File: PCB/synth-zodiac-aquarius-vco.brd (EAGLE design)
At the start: 160 x 100 mm, 47 parts, among them J3 3P, Male, Breakaway, 2.54mm, Q1 PMP4201, SW1 SPDT, U3 LM393, U4 TL074A, U5 CD4066

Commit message: Snapshot of designs so far.
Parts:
- removed C12: 4700pF, rlc:0603-CAP
- removed C13: 3900pF, rlc:0603-CAP
- removed C14: 22uF, rlc:0603-CAP
- removed C15: 100pF, rlc:0603-CAP
- removed C16: 1.0uF, rlc:0603-CAP
- removed C17: 220pF, rlc:0603-CAP
- removed C18, C19, C20, C21: 0.1uF, rlc:0603-CAP
- removed D3, D4: 1N4148, diodes:SOD-123
- removed J3: 3P, Male, Breakaway, 2.54mm, con-headers:MA03X1-VT-THD
- removed JMP56, JMP59, JMP60, R27, R28: 0, rlc:0603-RES
- removed JMP61: NS, rlc:0603-RES
- removed R25: 4.99K, rlc:0603-RES
- removed SW1: SPDT, switch-thd:SS-12-F45
- removed VCO_CORE: TPTHD-038, con-testpoints:THD-038MIL-X1
- removed VR1: 10K, rlc:ALPS_RK09D113
- removed VR10, VR5: 100K, rlc:TRIM_BOURNS_TC33X
- added BIAS: NP, rlc:TRIM_BOURNS_TC33X
- added C1: 4700pF, rlc:0603-CAP
- added C10: 220pF, rlc:0603-CAP
- added C2: 22uF, rlc:0603-CAP
- added C3, C4, C6, C7: 0.1uF, rlc:0603-CAP
- added C5: 3900pF, rlc:0603-CAP
- added C8: 1.0uF, rlc:0603-CAP
- added C9: 100pF, rlc:0603-CAP
- added CONST1: Aquarius, circuit-monkey-zodiac:AQUARIUS-CONST
- added CP_EXP_VCO, CP_GND, CP_VCO_LIN_FM, CP_VCO_OUT: PADSMD-070X070, con-testpoints:SMD-070MIL
- added D1, D2: 1N4148, diodes:SOD-123
- added EXP_VCO_TRIM: 100K - NP, rlc:TRIM_BOURNS_TC33X
- added FREQ: 10K, rlc:POT-RV9110
- added GLYPH: Aquarius, circuit-monkey-zodiac:AQUARIUS-GLYPH
- added J1: (no value), con-jst:B4B-PH-SM4
- added KB_CV, PWM_CV, VCO_MOD_CV, VCO_OUT: 2-pin, VT, SMT, con-jst:B2B-PH-SM4
- added KB_TRIM: 100K, rlc:TRIM_BOURNS_TC33X
- added PCB: PCB FAB, circuit-monkey-zodiac:PENTAGON-40MM-RAD
- added R2, R3: 221K, rlc:0603-RES
- added R20, R21, R22: 4.99K, rlc:0603-RES
- added R5: 68.1K - NP, rlc:0603-RES
- added R8: 1.82M, rlc:0603-RES
- added SAW: TPSMD-040-RND, con-testpoints:SMD-040MIL-RND
- added TYPE: SPDT, switch-thd:SS-12-F45-PNL-SMT
- PULSE, TP4: value TPTHD-038 -> TPSMD-040-RND; device con-testpoints:THD-038MIL-X1 -> con-testpoints:SMD-040MIL-RND
- R10: value 2.2K -> 0
- R11: value 499K -> 0
- R12: value 1.82M -> NS
- R13: value 10K -> 0
- R14: value 4.75M -> 0
- R15: value 10.0K -> 100K
- R16: value 4.99K -> 100K
- R17: value 4.99K -> 10.0K
- R18: value 4.99K -> 4.75M
- R19: value 10K -> 4.99K
- R23: value 100K -> 10K
- R24: value 100K -> 0
- R4: value 221K -> 412K
- R6: value 412K -> 2.2K
- R7: value 221K -> 499K
- R9: value 68.1K -> 10K
- moved PULSE 92.5 mm to (47.8, 48.4), flipped to the bottom, turned to 180 degrees
- moved R4 92.4 mm to (30.0, 41.1), flipped to the bottom, turned to 180 degrees
- moved R24 88.4 mm to (45.7, 44.4), flipped to the bottom
- moved TP4 86.2 mm to (50.8, 22.3), flipped to the bottom, turned to 180 degrees
- moved R6 79.3 mm to (46.0, 23.1), flipped to the bottom, turned to 180 degrees
- moved R7 73.1 mm to (46.0, 18.6), flipped to the bottom
- moved R19 71.8 mm to (22.2, 29.9), flipped to the bottom, turned to 180 degrees
- moved R13 68.8 mm to (46.0, 15.2), flipped to the bottom, turned to 180 degrees
- moved R18 68.2 mm to (30.0, 21.8), flipped to the bottom
- moved R9 66.6 mm to (30.0, 17.8), flipped to the bottom
- moved R14 66.0 mm to (46.0, 16.5), flipped to the bottom, turned to 180 degrees
- moved R17 65.2 mm to (30.0, 27.1), flipped to the bottom
- moved R15 64.2 mm to (54.0, 13.1), flipped to the bottom
- moved R11 62.1 mm to (15.5, 26.1), flipped to the bottom, turned to 180 degrees
- moved R12 60.6 mm to (15.5, 23.5), flipped to the bottom
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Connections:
- removed net N$10: R4.1, VR1.2
- removed net N$11: C12.1, R10.1, R4.2, R6.2, R7.2, R9.2, U4.2
- removed net N$19: J3.2, R16.2, R17.1, R18.1
- new net BIAS: BIAS.C, R19.2, R20.1, R21.1
- new net FREQ: FREQ.C, R2.1
- new net FREQ_CV_MIX: C1.1, R2.2, R3.2, R4.2, R5.2, R6.1, U4.2
- net +5V: now also C2.2, C5.1, J1.3, R16.2, R22.1; no longer C13.1, C14.2, R24.2, R25.1
- net +9V: now also C10.2, C3.2, C6.2, C7.2, FREQ.T, J1.1; no longer C17.2, C18.2, C19.2, C21.2, VR1.3
- net -9V: now also C4.1, FREQ.B, J1.2, R8.1; no longer C20.1, R12.1, VR1.1
- net EXP_VCO_CV_IN: now also CP_EXP_VCO.1, EXP_VCO_TRIM.B; no longer VR5.B
- net EXP_VCO_LIN_FM: now also CP_VCO_LIN_FM.1, R7.1; no longer R11.1
- net GND: now also BIAS.B, C2.1, C3.1, C4.2, C6.1, C7.1, C8.1, CP_GND.1, D2.A, J1.4, KB_CV.2, PCB.MTG1, PCB.MTG2, PCB.MTG3, PCB.MTG4, PCB.MTG5, PWM_CV.2, R10.1, R11.1, R14.1, R20.2, R23.2, R9.1, TYPE.MTG1, TYPE.MTG2, VCO_MOD_CV.2, VCO_OUT.2; no longer C14.1, C16.1, C18.1, C19.1, C20.2, C21.1, D4.A, J3.1, JMP59.1, JMP60.1, R17.2, R19.2, R27.1, R28.1, SW1.MT1A, SW1.MT1B, SW1.MT1C, SW1.MT2A, SW1.MT2B, SW1.MT2C, VR1.MT1A, VR1.MT1B, VR1.MT1C, VR1.MT2A, VR1.MT2B, VR1.MT2C
- net KB_CV: now also KB_CV.1, KB_TRIM.B; no longer VR10.B
- net N$12: now also R7.2, R8.2; no longer R11.2, R12.2
- net N$14: now also C1.2, R6.2; no longer C12.2, R10.2
- net N$15: now also R12.2, R9.2; no longer JMP61.2, R13.2
- net N$16: now also C9.1, R17.1, R18.1; no longer C15.1, R14.1, R15.1
- net N$17: now also R14.2; no longer R27.2
- net N$18: now also C9.2, D1.A, R18.2; no longer C15.2, D3.A, R14.2
- net N$20: now also C5.2; no longer C13.2
- net N$21: now also BIAS.T, C8.2, R17.2, R19.1; no longer C16.2, J3.3, R15.2, R16.1
- net N$22: now also C10.1, R21.2; no longer C17.1, R18.2
- net N$23: now also R12.1; no longer JMP61.1
- net N$24: now also D1.K, D2.K, R23.1; no longer D3.K, D4.K, R19.1
- net N$25: now also R10.2; no longer JMP60.2
- net N$26: now also R11.2; no longer JMP59.2
- net N$27: now also R13.2; no longer R28.2
- net N$28: now also R15.2, R16.1; no longer R23.2, R24.1
- net N$29: now also TP4.TP; no longer TP4.1
- net N$8: now also KB_TRIM.C, KB_TRIM.T, R4.1; no longer R6.1, VR10.C, VR10.T
- net N$9: now also EXP_VCO_TRIM.C, EXP_VCO_TRIM.T, R5.1; no longer R9.1, VR5.C, VR5.T
- net PULSE: now also PULSE.TP, R22.2, TYPE.B; no longer PULSE.1, R25.2, SW1.B
- net PWM_CV: now also PWM_CV.1, R15.1; no longer R23.1
- net SAW: now also R24.2, TYPE.A; no longer JMP56.2, SW1.A
- net VCO_CORE: now also R24.1, SAW.TP; no longer JMP56.1, VCO_CORE.1
- net VCO_MOD_CV: now also R3.1, VCO_MOD_CV.1; no longer R7.1
- net VCO_OUT: now also CP_VCO_OUT.1, TYPE.C, VCO_OUT.1; no longer SW1.C
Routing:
- net +9V: track 0.00 -> 98.5 mm, vias 0 -> 1
- net VCO_CORE: track 0.00 -> 84.1 mm, vias 0 -> 5
- net PULSE: track 0.00 -> 63.5 mm
- net +5V: track 0.00 -> 62.6 mm, vias 0 -> 3
- net VCO_OUT: track 0.00 -> 58.3 mm
- net FREQ_CV_MIX: track 0.00 -> 54.6 mm, vias 0 -> 5
- net -9V: track 0.00 -> 41.5 mm, vias 0 -> 2
- net N$20: track 0.00 -> 31.7 mm, vias 0 -> 2
- net N$15: track 0.00 -> 29.3 mm
- net N$22: track 0.00 -> 21.4 mm, vias 0 -> 2
- net PWM_CV: track 0.00 -> 20.3 mm
- net N$18: track 0.00 -> 17.7 mm, vias 0 -> 2
- net VCO_MOD_CV: track 0.00 -> 17.6 mm
- net N$16: track 0.00 -> 17.4 mm
- net KB_CV: track 0.00 -> 16.6 mm
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- added copper zone on layer 1, net GND
- added copper zone on layer 16, net GND
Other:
- board size 160 x 100 mm -> 76.1 x 72.4 mm
- board text added: "A Q U A R I U S"
- board text added: "S A T A N ' S C Y C L E W O R K S"
- board text added: "VCO"

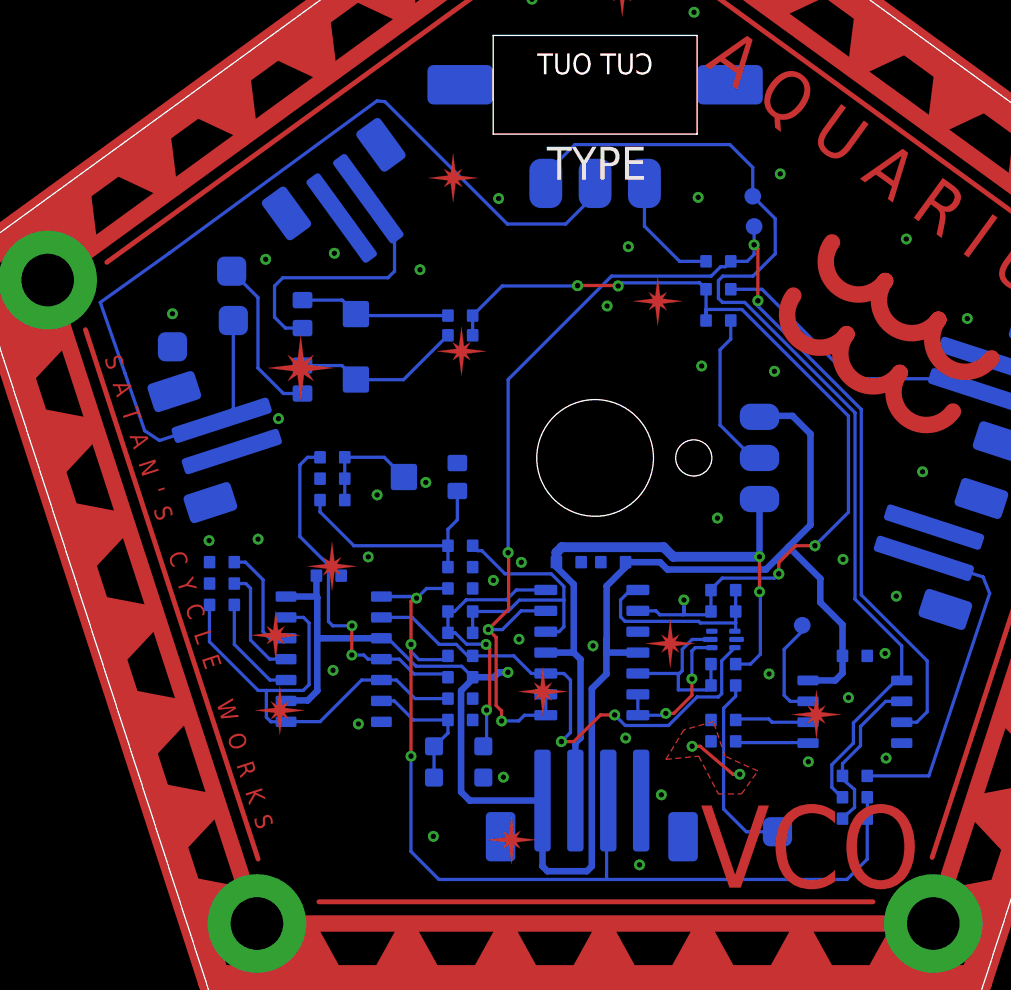
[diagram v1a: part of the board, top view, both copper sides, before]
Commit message: Almost ready for FAB.
Sagittarius was mis-spelled, renamed it.  Taurus is still WIP.
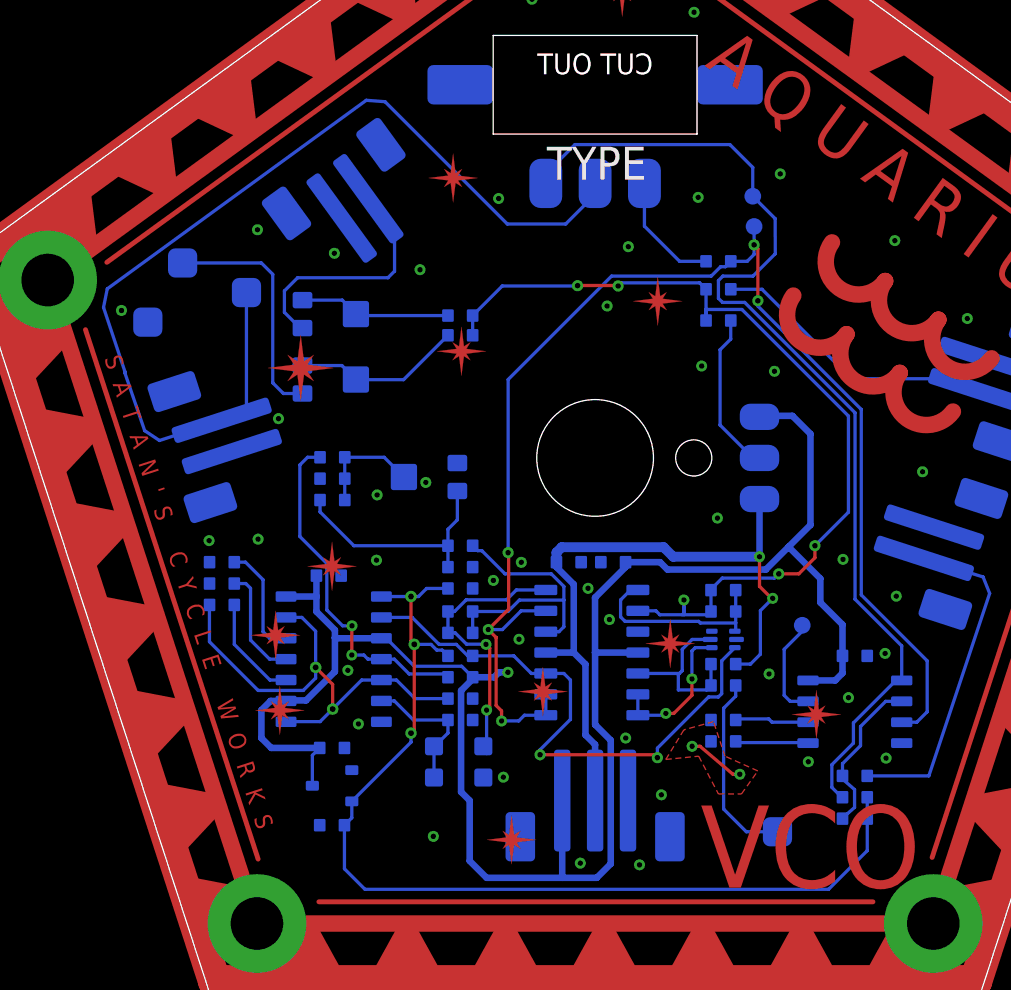
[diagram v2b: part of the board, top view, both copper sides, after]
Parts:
- removed J1: (no value), con-jst:B4B-PH-SM4
- removed U5: CD4066, logic:SOP14
- added C11, C12: 1uF, rlc:0603-CAP
- added PWR: JST, 3P, VT, SMT, con-jst:B3B-PH-SM4
- added U2: LM393, op-amp:SOP08
- added VR: 5V, regulators:SOT-23
- U3: value LM393 -> CD4066; device op-amp:SOP08 -> logic:SOP14
- moved U3 31.9 mm to (22.3, 20.2), turned to 0 degrees
- moved CP_EXP_VCO 4.03 mm to (12.6, 44.3), turned to 180 degrees
- moved CP_GND 2.12 mm to (11.5, 40.7)
- moved CP_VCO_OUT 1.88 mm to (17.5, 42.5)
- renumbered KB_CV to KB_IN, PWM_CV to VCO_MOD_PWM, U4 to U1, VCO_MOD_CV to VCO_MOD_IN, VCO_OUT to OUT2VCF
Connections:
- net +5V: now also C12.2, U3.1, VR.2; no longer J1.3, U5.1
- net +9V: now also C11.2, PWR.1, U2.8, U3.14, U3.3, U3.9, VR.3; no longer J1.1, U3.8, U5.14, U5.3, U5.9
- net -9V: now also PWR.2; no longer J1.2
- net GND: now also C11.1, C12.1, PWR.3, U2.4, U3.7, VR.1; no longer J1.4, U3.4, U5.7
- net N$15: now also U3.13, U3.5, U3.8; no longer U5.13, U5.5, U5.8
- net N$17: now also U2.6; no longer U3.6
- net N$20: now also U3.2; no longer U5.2
- net N$22: now also U3.4; no longer U5.4
- net N$23: now also U3.10; no longer U5.10
- net N$24: now also U3.6; no longer U5.6
- net N$25: now also U3.11; no longer U5.11
- net N$26: now also U3.12; no longer U5.12
- net N$27: now also U2.5; no longer U3.5
- net N$28: now also U2.2; no longer U3.2
- net N$29: now also U2.7; no longer U3.7
- net PULSE: now also U2.1; no longer U3.1
- net VCO_CORE: now also U2.3; no longer U3.3
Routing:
- net +9V: track 98.5 -> 114.2 mm
- net EXP_VCO_CV_IN: track 9.90 -> 14.4 mm
- net N$20: track 31.7 -> 34.6 mm
- net VCO_OUT: track 58.3 -> 60.8 mm
- net KB_CV: track 16.6 -> 15.1 mm
- net +5V: track 62.6 -> 61.5 mm
- net -9V: track 41.5 -> 42.4 mm
- net N$15: track 29.3 -> 29.6 mm, vias 0 -> 2
- net GND: vias 43 -> 45
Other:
- board text added: "Rev.A"

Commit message: Work in progress for rev A,  VCO rev.B
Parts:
- removed CP_EXP_VCO, CP_GND, CP_VCO_LIN_FM, CP_VCO_OUT: PADSMD-070X070, con-testpoints:SMD-070MIL
- removed EXP_VCO_TRIM: 100K - NP, rlc:TRIM_BOURNS_TC33X
- removed R24: 0, rlc:0603-RES
- removed TYPE: SPDT, switch-thd:SS-12-F45-PNL-SMT
- added F_0-5, F_GND: PADSMD-070X070, con-testpoints:SMD-070MIL
- added MODE: (no value), switch-thd:SS-12-F45-PNL-SMT
- added R1: 150K, rlc:0603-RES
- KB_IN, OUT2VCF, VCO_MOD_IN, VCO_MOD_PWM: value 2-pin, VT, SMT -> JST, SH, 2P; device con-jst:B2B-PH-SM4 -> con-jst:BM02B-SRSS-TB
- PWR: value JST, 3P, VT, SMT -> JST SM 3P; device con-jst:B3B-PH-SM4 -> con-jst:BM03B-SRSS-TB
- R5: value 68.1K - NP -> 150K
- R7: value 499K -> 47K
- moved R7 27.2 mm to (24.8, 35.7)
- moved VCO_MOD_PWM 13.9 mm to (54.7, 14.0)
- moved PWR 11.9 mm to (50.0, 10.8)
- moved R13 11.5 mm to (56.9, 19.0), turned to 0 degrees
- moved R14 11.0 mm to (56.9, 17.7), turned to 0 degrees
- moved C7 10.2 mm to (56.9, 30.2)
- moved R16 10.2 mm to (56.9, 20.3)
- moved R22 10.2 mm to (56.9, 21.6)
- moved U2 10.2 mm to (56.9, 26.8)
- moved R15 10.2 mm to (56.9, 22.9)
- moved C3 8.93 mm to (41.3, 17.4), turned to 0 degrees
- moved C4 8.88 mm to (38.4, 17.4), turned to 0 degrees
- moved U1 8.57 mm to (39.7, 12.2)
- moved C1 7.40 mm to (47.7, 17.2)
- moved R6 7.30 mm to (47.7, 16.0)
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- renumbered CONST1 to CONST
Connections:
- removed net EXP_VCO_CV_IN: CP_EXP_VCO.1, EXP_VCO_TRIM.B
- removed net EXP_VCO_LIN_FM: CP_VCO_LIN_FM.1, R7.1
- removed net N$9: EXP_VCO_TRIM.C, EXP_VCO_TRIM.T, R5.1
- removed net VCO_CORE: R24.1, SAW.TP, U1.13, U1.8, U1.9, U2.3
- new net FREQ_5: F_0-5.1, R1.1, R5.2, R7.2
- net +9V: now also R1.2
- net FREQ: now also R5.1
- net FREQ_CV_MIX: no longer R5.2
- net GND: now also F_GND.1, MODE.MTG1, MODE.MTG2, R7.1; no longer CP_GND.1, TYPE.MTG1, TYPE.MTG2
- net N$12: no longer R7.2
- net PULSE: now also MODE.B; no longer TYPE.B
- net SAW: now also MODE.A, SAW.TP, U1.13, U1.8, U1.9, U2.3; no longer R24.2, TYPE.A
- net VCO_OUT: now also MODE.C; no longer CP_VCO_OUT.1, TYPE.C
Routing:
- net VCO_CORE: track 84.1 -> 0.00 mm, vias 5 -> 0
- net SAW: track 7.23 -> 89.9 mm, vias 0 -> 6
- net FREQ: track 9.86 -> 32.2 mm
- net FREQ_5: track 0.00 -> 19.0 mm
- net EXP_VCO_CV_IN: track 14.4 -> 0.00 mm
- net +5V: track 61.5 -> 74.9 mm
- net N$18: track 17.7 -> 29.7 mm
- net VCO_OUT: track 60.8 -> 48.9 mm
- net EXP_VCO_LIN_FM: track 11.7 -> 0.00 mm
- net N$9: track 10.3 -> 0.00 mm
- net +9V: track 114.2 -> 123.2 mm, vias 1 -> 2
- net -9V: track 42.4 -> 51.2 mm
- net N$17: track 4.51 -> 11.6 mm
- net KB_CV: track 15.1 -> 8.49 mm
- net PULSE: track 63.5 -> 57.2 mm
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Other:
- board text added: "Rev.B"
- board text removed: "Rev.A"
